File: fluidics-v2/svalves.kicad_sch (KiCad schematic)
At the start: 0 parts

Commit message: new version
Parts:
- added C3 (x2): 1u, Capacitor_SMD:C_0603_1608Metric, symbol Device:C
- added C4: 0.01u, Capacitor_SMD:C_0603_1608Metric, symbol Device:C
- added C4 (x2): 0.1u, Capacitor_SMD:C_0603_1608Metric, symbol Device:C
- added IC2: ADUM1250WSRZ-RL7, analog_devices:SOIC127P600X175-8N, symbol analog_devices:ADUM1250WSRZ-RL7
- added R1, R2: 10k, Resistor_SMD:R_0402_1005Metric, symbol Device:R
- added U12: LTC4311CSC6-TRPBF, SOT-6_SC_LIT, symbol LTC4311CSC6#TRPBF:LTC4311CSC6-TRPBF
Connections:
- new net +3.3V: C3.1, C4.1, IC2.1 (VDD1)
- new net +5V: C3.1, C4.1, C4.1, IC2.8 (VDD2), R1.1, R2.1, U12.1 (VCC), U12.3 (ENABLE)
- new net GND: C3.2, C3.2, C4.2, C4.2, C4.2, IC2.4 (GND1), IC2.5 (GND2), U12.2 (GND), U12.5 (GND)
- new net SCL 3.3V: IC2.3 (SCL1)
- new net SCL 5V: IC2.6 (SCL2), R2.2, U12.6 (BUS1)
- new net SDA 3.3V: IC2.2 (SDA1)
- new net SDA 5V: IC2.7 (SDA2), R1.2, U12.4 (BUS2)
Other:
- removed sheet UART Level Shift0
- removed sheet UART Level Shift1
- removed sheet UART Level Shift2
- removed sheet UART Level Shift3
- removed sheet UART Level Shift4
- note added: "3.3V <-> 5V level shifter"
- note added: "Active Pullup - increase number of devices connected at once and length of cable"
- note added: "Pullup resistors"

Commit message: started layout
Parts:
- U7: renamed from U12; footprint SOT-6_SC_LIT -> LTC:SOT-6_SC_LIT-L
- renumbered C4 to C?, C3 to C?, R2 to R?, R1 to R?

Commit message: added pressure controllers and more flow sensors
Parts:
- C? (x2): footprint Capacitor_SMD:C_0603_1608Metric -> Capacitor_SMD:C_0805_2012Metric
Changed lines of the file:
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@@
       (effects (font (size 1.27 1.27)) (justify left))
     )
-    (property "Footprint" "Capacitor_SMD:C_0603_1608Metric" (at 60.6552 46.99 0)
+    (property "Footprint" "Capacitor_SMD:C_0805_2012Metric" (at 60.6552 46.99 0)
       (effects (font (size 1.27 1.27)) hide)
     )
@@
       (effects (font (size 1.27 1.27)) (justify left))
     )
-    (property "Footprint" "Capacitor_SMD:C_0603_1608Metric" (at 96.8248 46.99 0)
+    (property "Footprint" "Capacitor_SMD:C_0805_2012Metric" (at 96.8248 46.99 0)
       (effects (font (size 1.27 1.27)) hide)
     )

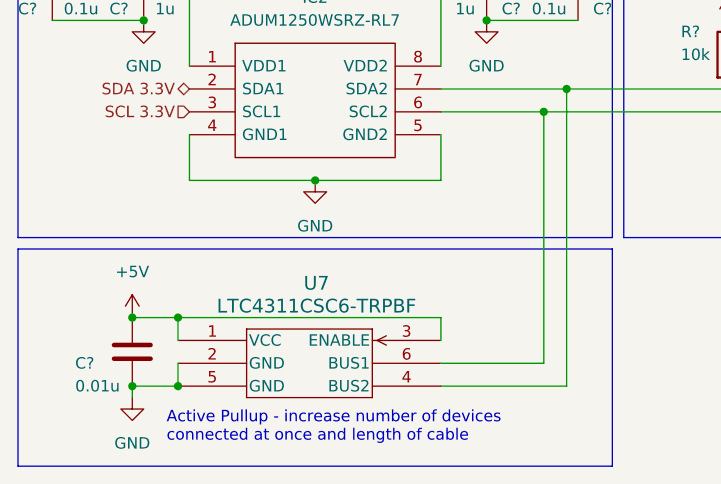
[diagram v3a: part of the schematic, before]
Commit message: added new connector for motor control daughter board. began layout
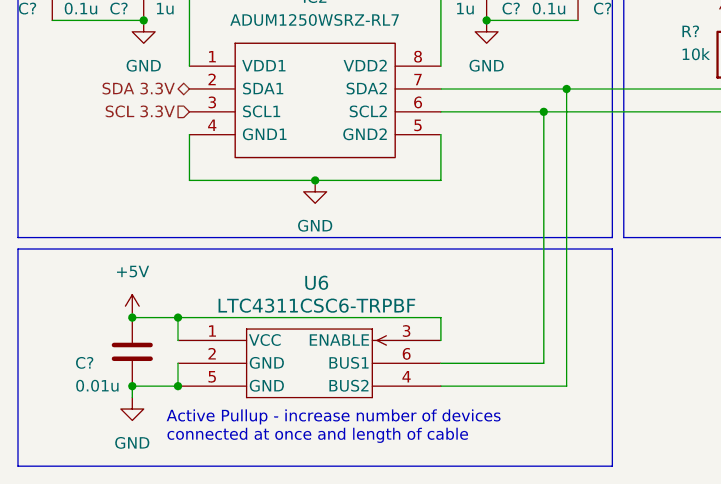
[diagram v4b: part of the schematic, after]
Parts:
- renumbered U7 to U6
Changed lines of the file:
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@@
         )
         (path "/0ec91c42-8aad-437d-8c85-5e10f0e51fe0/7edd626f-fd99-40ee-aab3-2aaadfd0b2bc"
-          (reference "C7") (unit 1)
+          (reference "C6") (unit 1)
         )
       )
@@
   (symbol (lib_id "power:+5V") (at 97.79 39.37 0) (unit 1)
     (in_bom yes) (on_board yes) (dnp no) (fields_autoplaced)
-    (property "Reference" "#PWR080" (at 97.79 43.18 0)
+    (property "Reference" "#PWR091" (at 97.79 43.18 0)
       (effects (font (size 1.27 1.27)) hide)
     )
@@
       (project "fluidics-v2"
         (path "/0ec91c42-8aad-437d-8c85-5e10f0e51fe0/7edd626f-fd99-40ee-aab3-2aaadfd0b2bc"
-          (reference "#PWR080") (unit 1)
+          (reference "#PWR091") (unit 1)
         )
       )
@@
   (symbol (lib_id "power:GND") (at 59.69 46.99 0) (unit 1)
     (in_bom yes) (on_board yes) (dnp no) (fields_autoplaced)
-    (property "Reference" "#PWR078" (at 59.69 53.34 0)
+    (property "Reference" "#PWR089" (at 59.69 53.34 0)
       (effects (font (size 1.27 1.27)) hide)
     )
@@
       (project "fluidics-v2"
         (path "/0ec91c42-8aad-437d-8c85-5e10f0e51fe0/7edd626f-fd99-40ee-aab3-2aaadfd0b2bc"
-          (reference "#PWR078") (unit 1)
+          (reference "#PWR089") (unit 1)
         )
       )
@@
         )
         (path "/0ec91c42-8aad-437d-8c85-5e10f0e51fe0/7edd626f-fd99-40ee-aab3-2aaadfd0b2bc"
-          (reference "C6") (unit 1)
+          (reference "C5") (unit 1)
         )
       )
@@
         )
         (path "/0ec91c42-8aad-437d-8c85-5e10f0e51fe0/7edd626f-fd99-40ee-aab3-2aaadfd0b2bc"
-          (reference "R25") (unit 1)
+          (reference "R23") (unit 1)
         )
       )
@@
   (symbol (lib_id "power:+5V") (at 124.46 46.99 0) (unit 1)
     (in_bom yes) (on_board yes) (dnp no) (fields_autoplaced)
-    (property "Reference" "#PWR082" (at 124.46 50.8 0)
+    (property "Reference" "#PWR093" (at 124.46 50.8 0)
       (effects (font (size 1.27 1.27)) hide)
     )
@@
       (project "fluidics-v2"
         (path "/0ec91c42-8aad-437d-8c85-5e10f0e51fe0/7edd626f-fd99-40ee-aab3-2aaadfd0b2bc"
-          (reference "#PWR082") (unit 1)
+          (reference "#PWR093") (unit 1)
         )
       )
@@
   (symbol (lib_id "power:GND") (at 97.79 46.99 0) (mirror y) (unit 1)
     (in_bom yes) (on_board yes) (dnp no) (fields_autoplaced)
-    (property "Reference" "#PWR081" (at 97.79 53.34 0)
+    (property "Reference" "#PWR092" (at 97.79 53.34 0)
       (effects (font (size 1.27 1.27)) hide)
     )
@@
       (project "fluidics-v2"
         (path "/0ec91c42-8aad-437d-8c85-5e10f0e51fe0/7edd626f-fd99-40ee-aab3-2aaadfd0b2bc"
-          (reference "#PWR081") (unit 1)
+          (reference "#PWR092") (unit 1)
         )
       )
@@
   (symbol (lib_id "power:+3.3V") (at 59.69 39.37 0) (unit 1)
     (in_bom yes) (on_board yes) (dnp no) (fields_autoplaced)
-    (property "Reference" "#PWR077" (at 59.69 43.18 0)
+    (property "Reference" "#PWR088" (at 59.69 43.18 0)
       (effects (font (size 1.27 1.27)) hide)
     )
@@
       (project "fluidics-v2"
         (path "/0ec91c42-8aad-437d-8c85-5e10f0e51fe0/7edd626f-fd99-40ee-aab3-2aaadfd0b2bc"
-          (reference "#PWR077") (unit 1)
+          (reference "#PWR088") (unit 1)
         )
       )
@@
         )
         (path "/0ec91c42-8aad-437d-8c85-5e10f0e51fe0/7edd626f-fd99-40ee-aab3-2aaadfd0b2bc"
-          (reference "C8") (unit 1)
+          (reference "C7") (unit 1)
         )
       )
@@
   (symbol (lib_id "power:+5V") (at 128.27 49.53 0) (unit 1)
     (in_bom yes) (on_board yes) (dnp no) (fields_autoplaced)
-    (property "Reference" "#PWR083" (at 128.27 53.34 0)
+    (property "Reference" "#PWR094" (at 128.27 53.34 0)
       (effects (font (size 1.27 1.27)) hide)
     )
@@
       (project "fluidics-v2"
         (path "/0ec91c42-8aad-437d-8c85-5e10f0e51fe0/7edd626f-fd99-40ee-aab3-2aaadfd0b2bc"
-          (reference "#PWR083") (unit 1)
+          (reference "#PWR094") (unit 1)
         )
       )
@@
   (symbol (lib_id "power:+5V") (at 58.42 80.01 0) (unit 1)
     (in_bom yes) (on_board yes) (dnp no) (fields_autoplaced)
-    (property "Reference" "#PWR075" (at 58.42 83.82 0)
+    (property "Reference" "#PWR086" (at 58.42 83.82 0)
       (effects (font (size 1.27 1.27)) hide)
     )
@@
       (project "fluidics-v2"
         (path "/0ec91c42-8aad-437d-8c85-5e10f0e51fe0/7edd626f-fd99-40ee-aab3-2aaadfd0b2bc"
-          (reference "#PWR075") (unit 1)
+          (reference "#PWR086") (unit 1)
         )
       )
@@
         )
         (path "/0ec91c42-8aad-437d-8c85-5e10f0e51fe0/7edd626f-fd99-40ee-aab3-2aaadfd0b2bc"
-          (reference "C9") (unit 1)
+          (reference "C8") (unit 1)
         )
       )
@@
         )
         (path "/0ec91c42-8aad-437d-8c85-5e10f0e51fe0/7edd626f-fd99-40ee-aab3-2aaadfd0b2bc"
-          (reference "R24") (unit 1)
+          (reference "R22") (unit 1)
         )
       )
@@
   (symbol (lib_id "power:GND") (at 58.42 88.9 0) (unit 1)
     (in_bom yes) (on_board yes) (dnp no) (fields_autoplaced)
-    (property "Reference" "#PWR076" (at 58.42 95.25 0)
+    (property "Reference" "#PWR087" (at 58.42 95.25 0)
       (effects (font (size 1.27 1.27)) hide)
     )
@@
       (project "fluidics-v2"
         (path "/0ec91c42-8aad-437d-8c85-5e10f0e51fe0/7edd626f-fd99-40ee-aab3-2aaadfd0b2bc"
-          (reference "#PWR076") (unit 1)
+          (reference "#PWR087") (unit 1)
         )
       )
@@
   (symbol (lib_id "power:GND") (at 78.74 64.77 0) (unit 1)
     (in_bom yes) (on_board yes) (dnp no) (fields_autoplaced)
-    (property "Reference" "#PWR079" (at 78.74 71.12 0)
+    (property "Reference" "#PWR090" (at 78.74 71.12 0)
       (effects (font (size 1.27 1.27)) hide)
     )
@@
       (project "fluidics-v2"
         (path "/0ec91c42-8aad-437d-8c85-5e10f0e51fe0/7edd626f-fd99-40ee-aab3-2aaadfd0b2bc"
-          (reference "#PWR079") (unit 1)
+          (reference "#PWR090") (unit 1)
         )
       )
@@
   (symbol (lib_id "LTC4311CSC6#TRPBF:LTC4311CSC6-TRPBF") (at 77.47 85.09 0) (unit 1)
     (in_bom yes) (on_board yes) (dnp no) (fields_autoplaced)
-    (property "Reference" "U7" (at 78.886 76.2 0)
+    (property "Reference" "U6" (at 78.886 76.2 0)
       (effects (font (size 1.524 1.524)))
     )
@@
       (project "fluidics-v2"
         (path "/0ec91c42-8aad-437d-8c85-5e10f0e51fe0/7edd626f-fd99-40ee-aab3-2aaadfd0b2bc"
-          (reference "U7") (unit 1)
+          (reference "U6") (unit 1)
         )
       )
@@
         )
         (path "/0ec91c42-8aad-437d-8c85-5e10f0e51fe0/7edd626f-fd99-40ee-aab3-2aaadfd0b2bc"
-          (reference "C10") (unit 1)
-        )
-      )
+          (reference "C9") (unit 1)
+        )
+      )

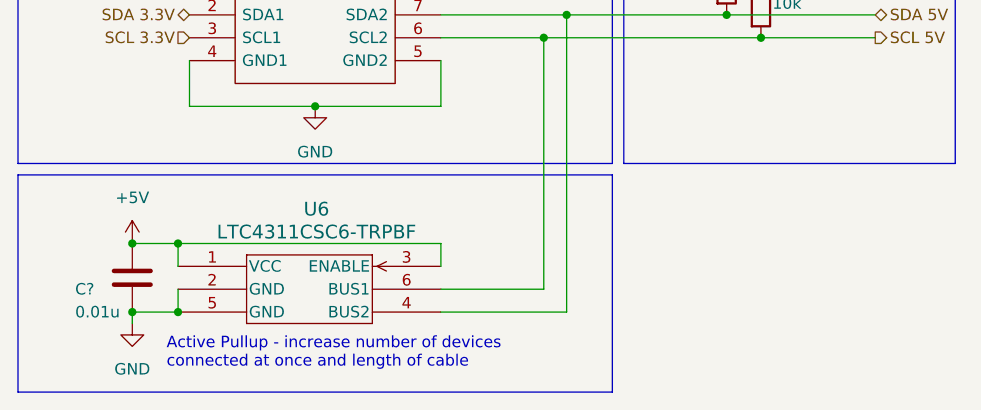
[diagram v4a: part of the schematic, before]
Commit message: added pullups/downs to spi for stability, rounded corners
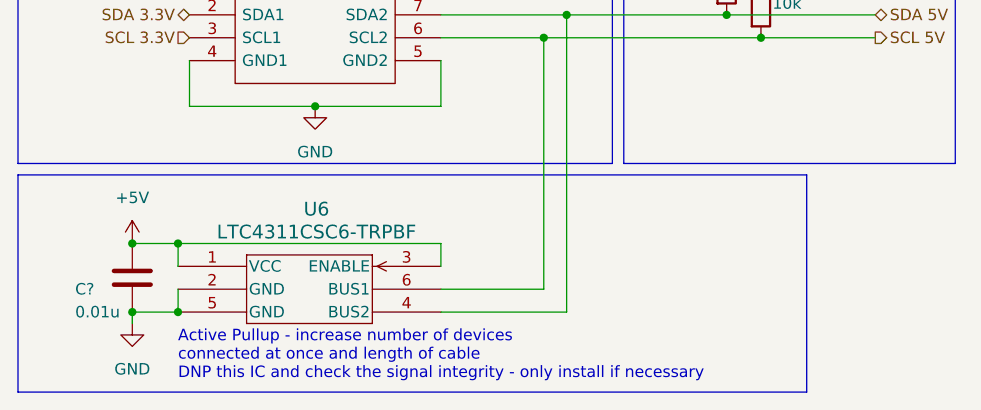
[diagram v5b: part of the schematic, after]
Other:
- note added: "Active Pullup - increase number of devices connected at once and length of cable DNP this IC and check the signal integrity - only install if necessary"
- note removed: "Active Pullup - increase number of devices connected at once and length of cable"
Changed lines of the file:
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@@
     (stroke (width 0) (type default))
   )
-  (rectangle (start 45.72 72.39) (end 111.76 96.52)
+  (rectangle (start 45.72 72.39) (end 133.35 96.52)
     (stroke (width 0) (type default))
     (fill (type none))
@@
     (effects (font (size 1.27 1.27)) (justify left bottom))
   )
-  (text "Active Pullup - increase number of devices \nconnected at once and length of cable"
-    (at 62.23 93.98 0)
+  (text "Active Pullup - increase number of devices \nconnected at once and length of cable\nDNP this IC and check the signal integrity - only install if necessary"
+    (at 63.5 95.25 0)
     (effects (font (size 1.27 1.27)) (justify left bottom))
   )
